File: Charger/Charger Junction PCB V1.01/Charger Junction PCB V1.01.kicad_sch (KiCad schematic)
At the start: 2 parts

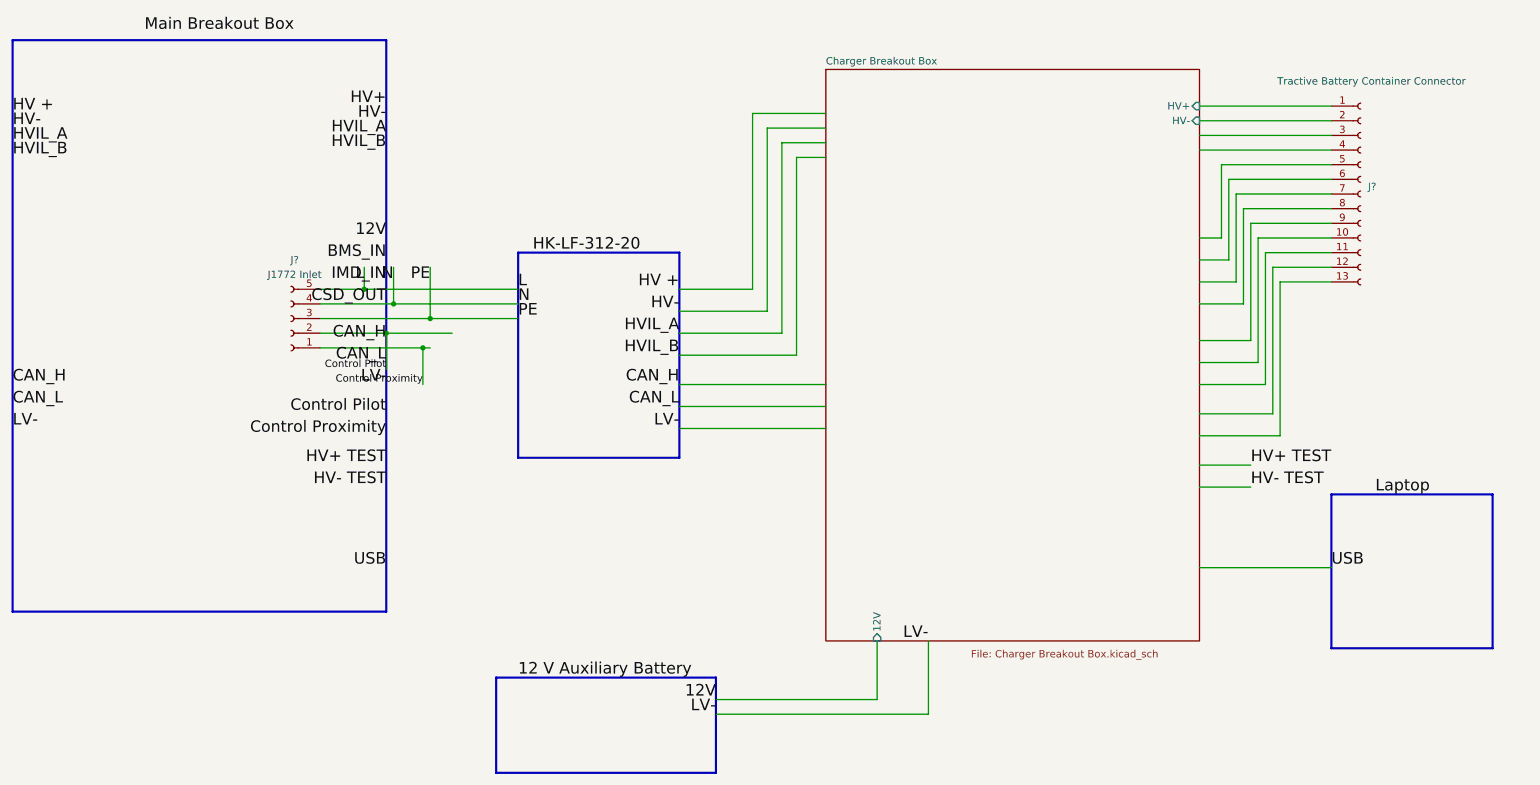
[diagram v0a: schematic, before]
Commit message: Added different KiCad project for block diagram, renamed project file, added J1772 circuit
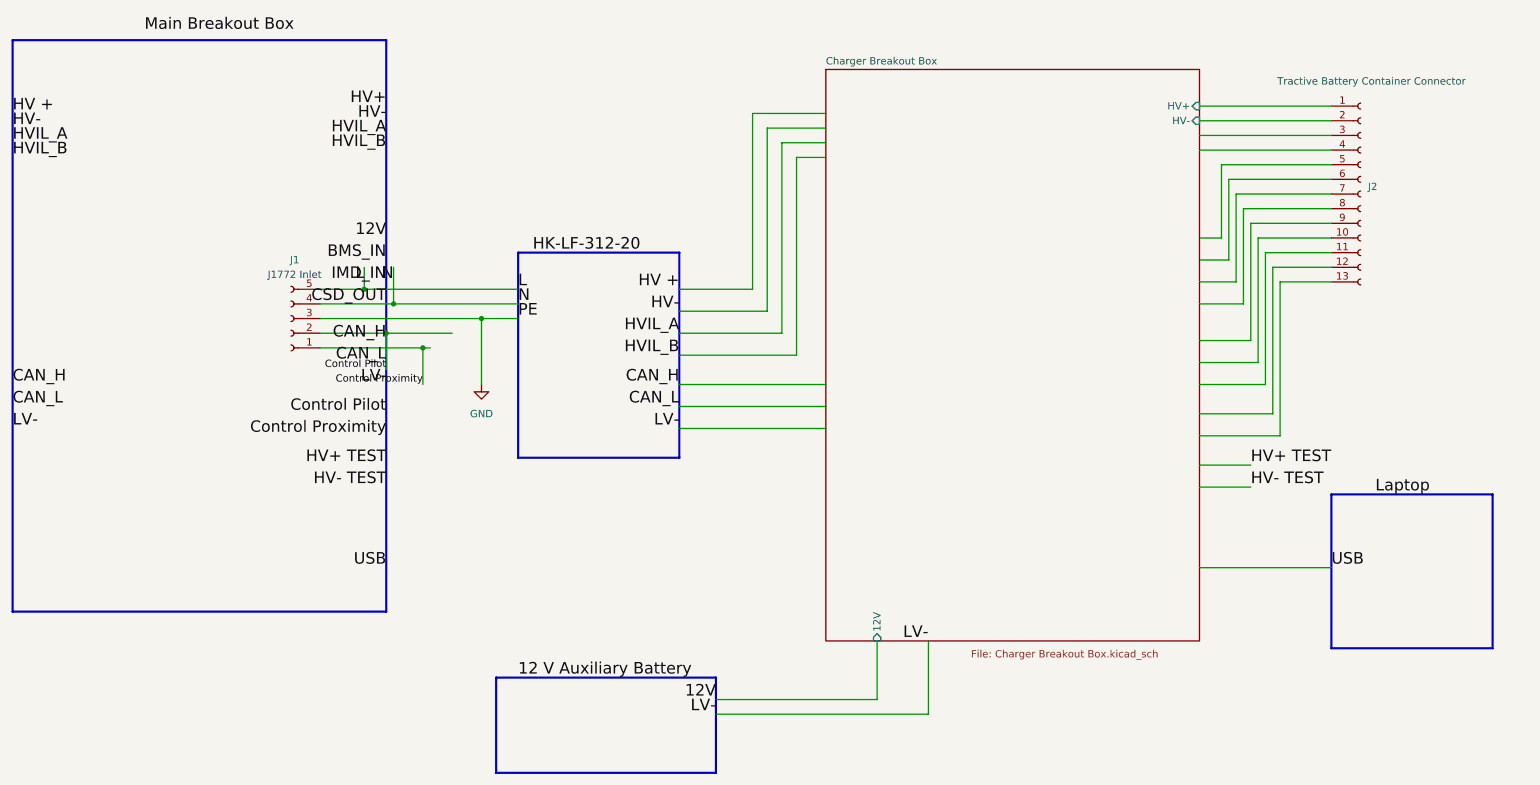
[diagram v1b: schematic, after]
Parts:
- gave numbers to parts that had none: 2
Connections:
- net PE renamed GND
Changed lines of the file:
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@@
 	)
 	(junction
-		(at 91.44 88.9)
+		(at 100.33 88.9)
 		(diameter 0)
 		(color 0 0 0 0)
@@
 	(wire
 		(pts
-			(xy 91.44 88.9) (xy 106.68 88.9)
-		)
-		(stroke
-			(width 0)
-			(type default)
-		)
-	)
-	(wire
-		(pts
 			(xy 228.6 62.23) (xy 228.6 74.93)
 		)
@@
 	(wire
 		(pts
+			(xy 100.33 88.9) (xy 100.33 100.33)
+		)
+		(stroke
+			(width 0)
+			(type default)
+		)
+	)
+	(wire
+		(pts
 			(xy 134.62 107.95) (xy 160.02 107.95)
 		)
@@
 	(wire
 		(pts
+			(xy 100.33 88.9) (xy 106.68 88.9)
+		)
+		(stroke
+			(width 0)
+			(type default)
+		)
+	)
+	(wire
+		(pts
 			(xy 224.79 105.41) (xy 237.49 105.41)
 		)
@@
 	(wire
 		(pts
-			(xy 91.44 80.01) (xy 91.44 88.9)
-		)
-		(stroke
-			(width 0)
-			(type default)
-		)
-	)
-	(wire
-		(pts
 			(xy 168.91 144.78) (xy 168.91 154.94)
 		)
@@
 	(wire
 		(pts
-			(xy 72.39 88.9) (xy 91.44 88.9)
+			(xy 72.39 88.9) (xy 100.33 88.9)
 		)
 		(stroke
@@
 		)
 	)
-	(label "PE"
-		(at 91.44 82.55 180)
-		(effects
-			(font
-				(size 2 2)
-			)
-			(justify right bottom)
-		)
-	)
 	(label "HVIL_A"
 		(at 83.82 57.15 180)
@@
 			)
 			(justify left bottom)
+		)
+	)
+	(symbol
+		(lib_id "power:GND")
+		(at 100.33 100.33 0)
+		(unit 1)
+		(body_style 1)
+		(exclude_from_sim no)
+		(in_bom yes)
+		(on_board yes)
+		(in_pos_files yes)
+		(dnp no)
+		(fields_autoplaced yes)
+		(property "Reference" "#PWR01"
+			(at 100.33 106.68 0)
+			(hide yes)
+			(show_name no)
+			(do_not_autoplace no)
+			(effects
+				(font
+					(size 1.27 1.27)
+				)
+			)
+		)
+		(property "Value" "GND"
+			(at 100.33 105.41 0)
+			(show_name no)
+			(do_not_autoplace no)
+			(effects
+				(font
+					(size 1.27 1.27)
+				)
+			)
+		)
+		(property "Footprint" ""
+			(at 100.33 100.33 0)
+			(hide yes)
+			(show_name no)
+			(do_not_autoplace no)
+			(effects
+				(font
+					(size 1.27 1.27)
+				)
+			)
+		)
+		(property "Datasheet" ""
+			(at 100.33 100.33 0)
+			(hide yes)
+			(show_name no)
+			(do_not_autoplace no)
+			(effects
+				(font
+					(size 1.27 1.27)
+				)
+			)
+		)
+		(property "Description" "Power symbol creates a global label with name \"GND\" , ground"
+			(at 100.33 100.33 0)
+			(hide yes)
+			(show_name no)
+			(do_not_autoplace no)
+			(effects
+				(font
+					(size 1.27 1.27)
+				)
+			)
+		)
+		(pin "1"
+		)
+		(instances
+			(project "Charger Master"
+				(path "/75f6fa4d-fba8-4d29-9299-863888d8bb95"
+					(reference "#PWR01")
+					(unit 1)
+				)
+			)
 		)
 	)
@@
 		(in_pos_files yes)
 		(dnp no)
-		(property "Reference" "J?"
+		(property "Reference" "J2"
 			(at 254 66.0399 0)
 			(show_name no)
@@
 			(project "Charger Master"
 				(path "/75f6fa4d-fba8-4d29-9299-863888d8bb95"
-					(reference "J?")
+					(reference "J2")
 					(unit 1)
 				)
@@
 		(dnp no)
 		(fields_autoplaced yes)
-		(property "Reference" "J?"
+		(property "Reference" "J1"
 			(at 67.945 78.74 0)
 			(show_name no)
@@
 			(project "Charger Master"
 				(path "/75f6fa4d-fba8-4d29-9299-863888d8bb95"
-					(reference "J?")
+					(reference "J1")
 					(unit 1)
 				)
